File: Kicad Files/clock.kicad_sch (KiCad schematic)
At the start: 33 parts

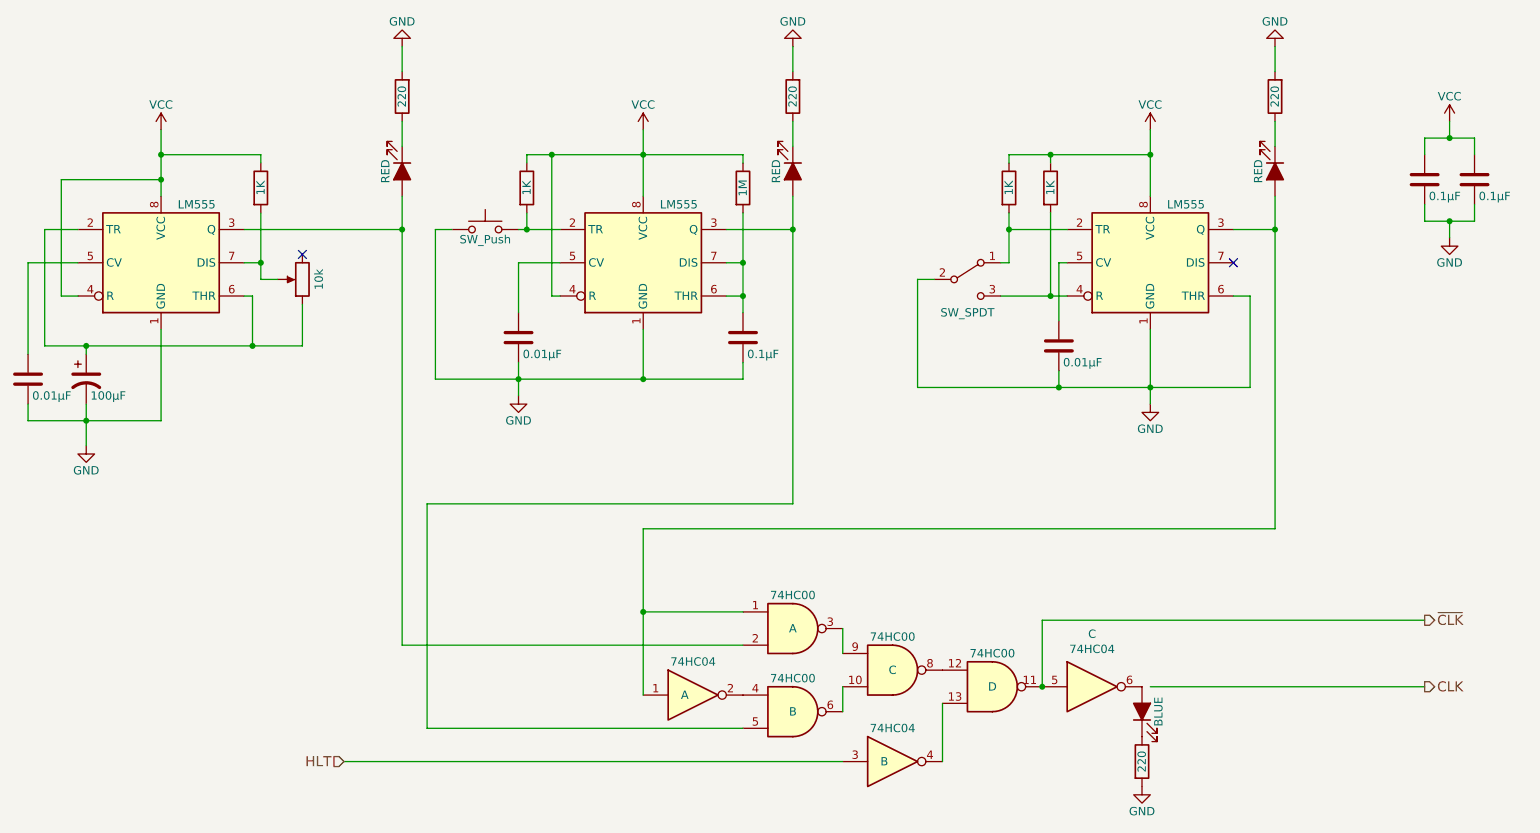
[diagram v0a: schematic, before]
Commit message: started tidy up in control
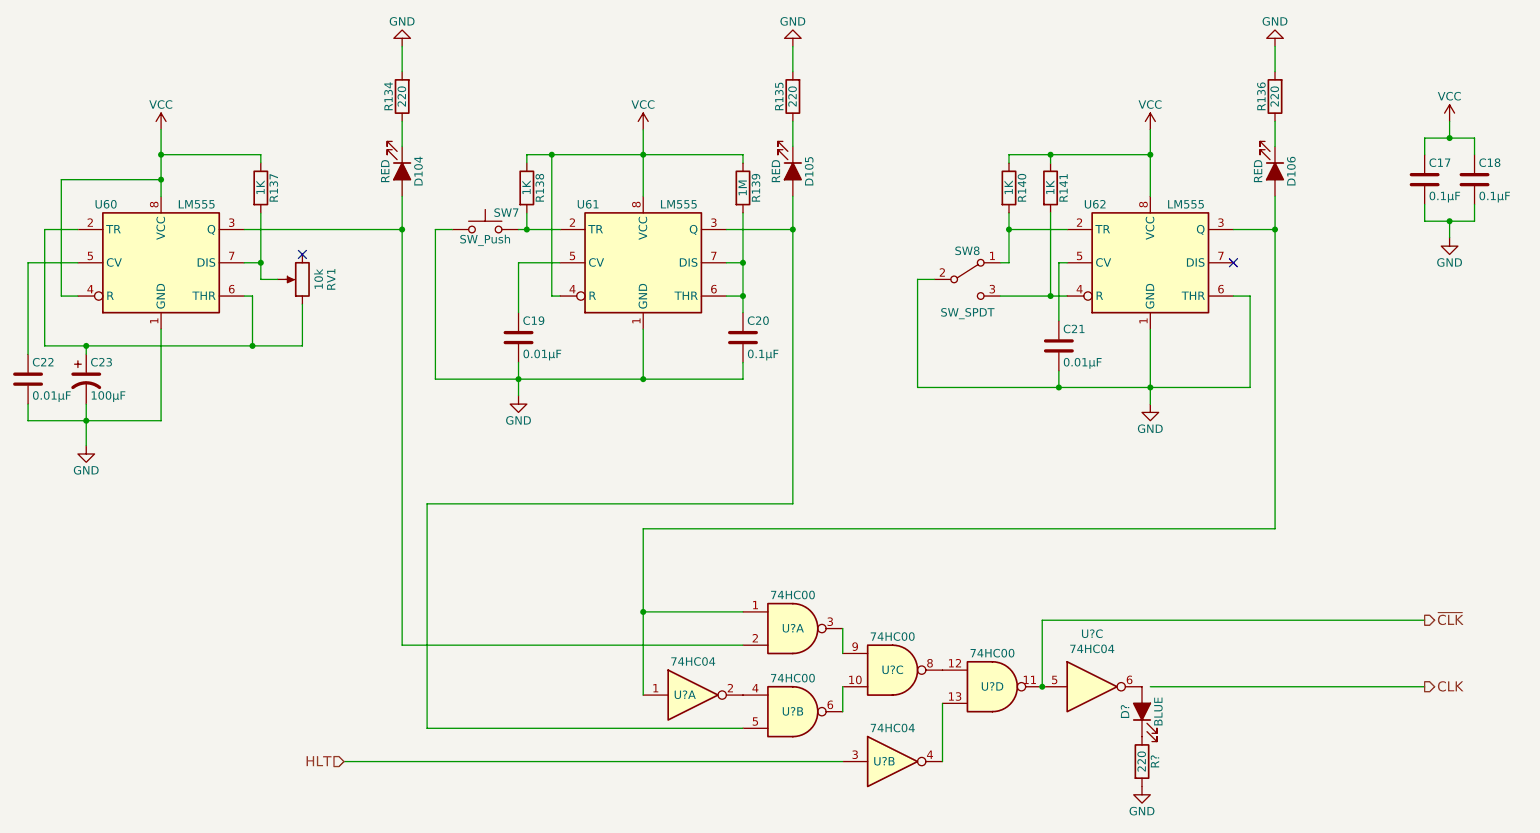
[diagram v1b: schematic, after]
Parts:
- gave numbers to parts that had none: 27

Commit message: work on cl
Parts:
- C3: renamed from C22; value 0.01µF -> C
- C5: renamed from C19; value 0.01µF -> C
- C6: renamed from C20; value 0.1µF -> C
- C7: renamed from C21; value 0.01µF -> C
- C8: renamed from C17; value 0.1µF -> C
- C9: renamed from C18; value 0.1µF -> C
- R37: renamed from R137; value 1K -> R
- R38: renamed from R134; value 220 -> R
- R39: renamed from R138; value 1K -> R
- R40: renamed from R139; value 1M -> R
- R41: renamed from R135; value 220 -> R
- R42: renamed from R140; value 1K -> R
- R43: renamed from R141; value 1K -> R
- R44: renamed from R?; value 220 -> R
- R45: renamed from R136; value 220 -> R
- gave numbers to parts that had none: 3
- renumbered C23 to C4, D104 to D12, D105 to D13, D106 to D15, SW7 to SW6, SW8 to SW7, U62 to U12, U60 to U8, U61 to U9

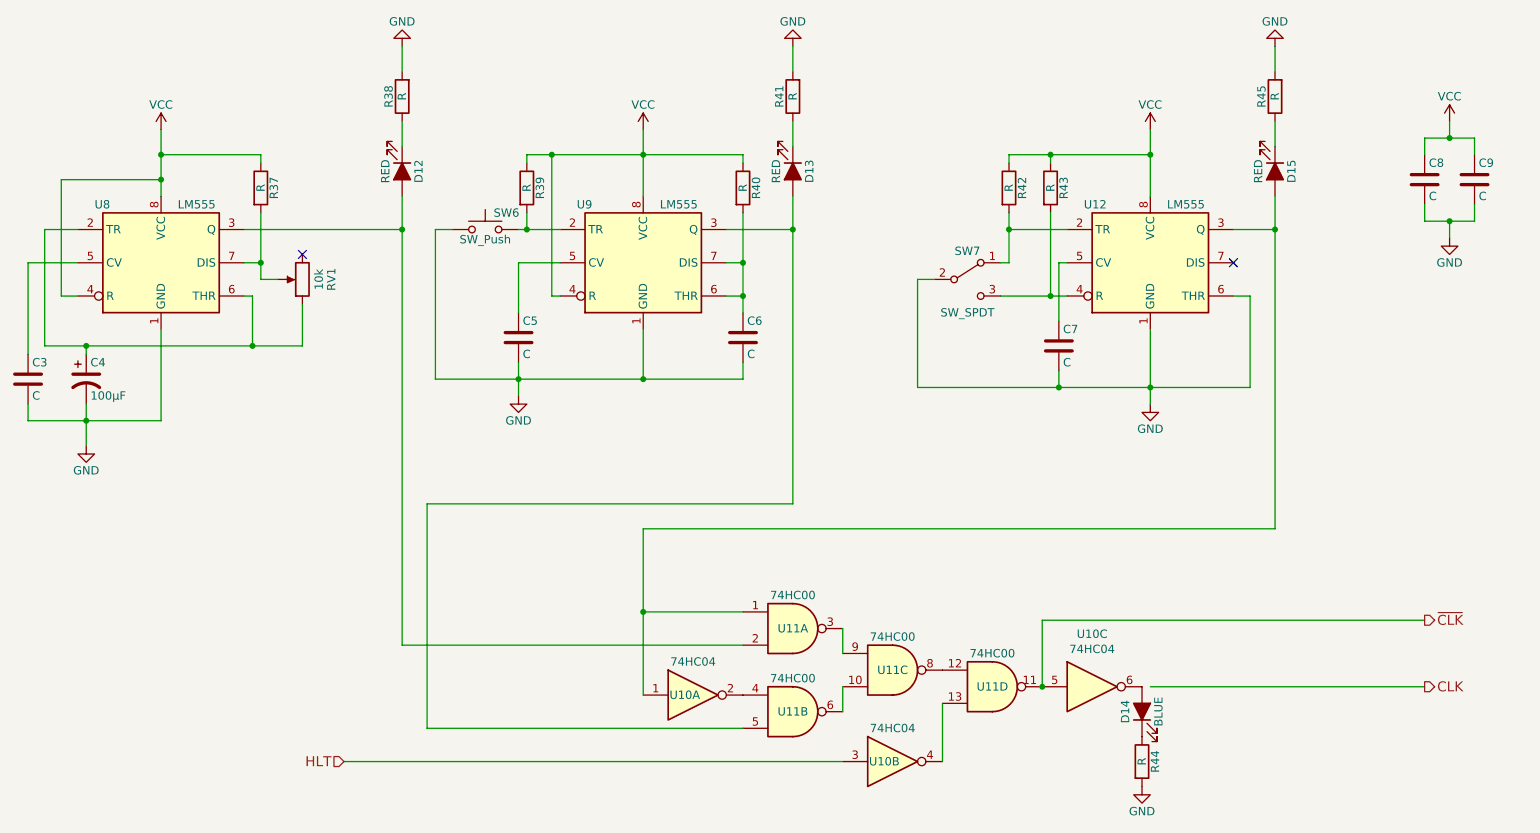
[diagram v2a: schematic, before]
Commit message: fixed ecc problems
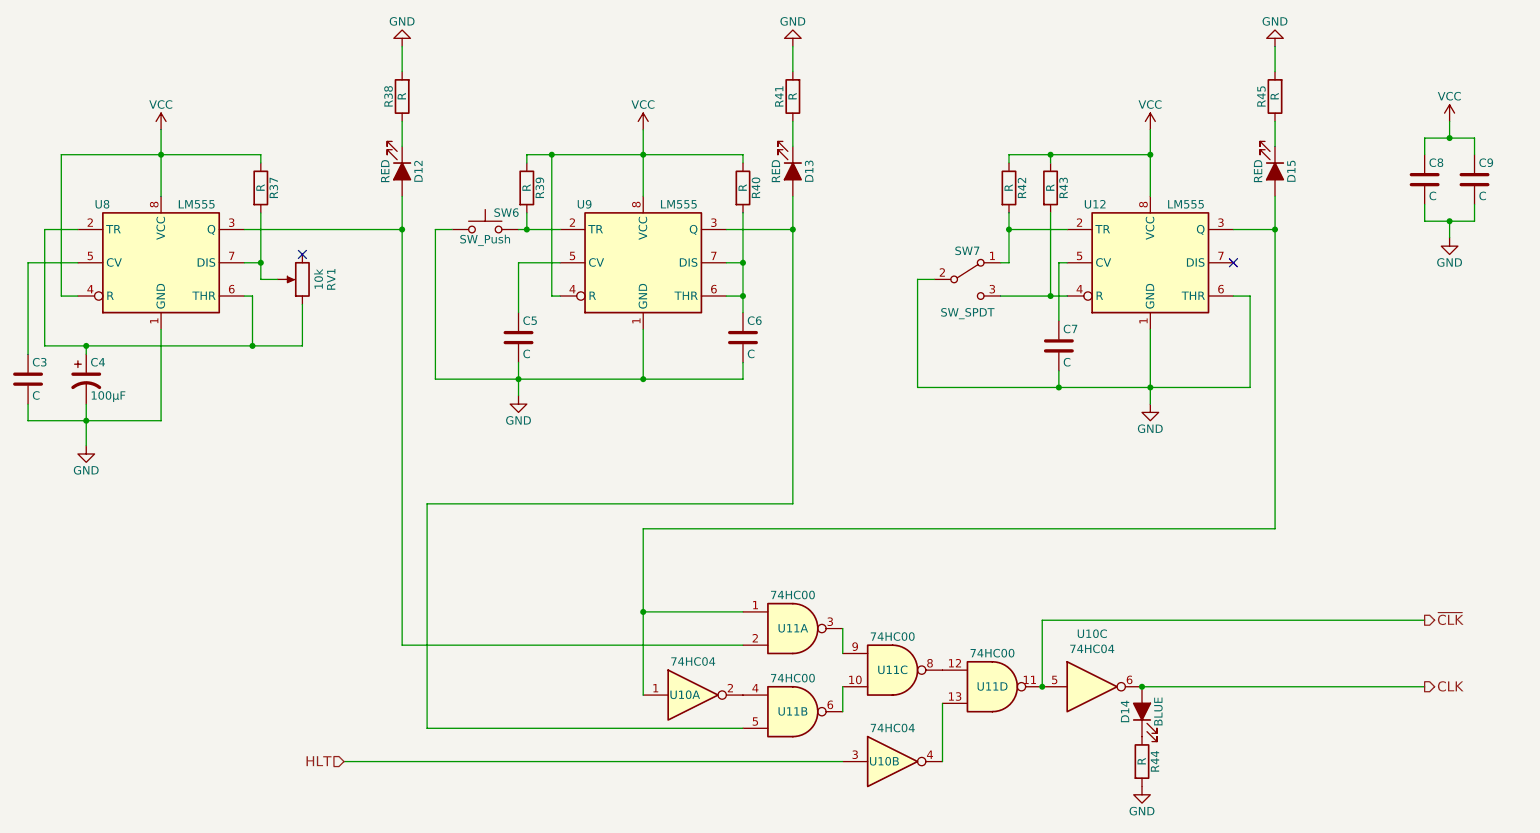
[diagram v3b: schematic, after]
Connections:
- net CLK: now also D14.2 (A), U10.6
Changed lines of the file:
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@@
   (junction (at 247.65 46.99) (diameter 0) (color 0 0 0 0)
   )
-  (junction (at 50.8 40.64) (diameter 0) (color 0 0 0 0)
-  )
   (junction (at 247.65 34.29) (diameter 0) (color 0 0 0 0)
   )
@@
   )
   (junction (at 87.63 48.26) (diameter 0) (color 0 0 0 0)
+  )
+  (junction (at 200.66 118.11) (diameter 0) (color 0 0 0 0)
   )
   (junction (at 124.46 71.12) (diameter 0) (color 0 0 0 0)
@@
     (stroke (width 0) (type default) (color 0 0 0 0))
   )
-  (wire (pts (xy 35.56 58.42) (xy 35.56 40.64))
+  (wire (pts (xy 35.56 58.42) (xy 35.56 36.83))
     (stroke (width 0) (type default) (color 0 0 0 0))
   )
@@
     (stroke (width 0) (type default) (color 0 0 0 0))
   )
-  (wire (pts (xy 201.93 118.11) (xy 243.84 118.11))
+  (wire (pts (xy 200.66 118.11) (xy 243.84 118.11))
     (stroke (width 0) (type default) (color 0 0 0 0))
   )
@@
     (stroke (width 0) (type default) (color 0 0 0 0))
   )
-  (wire (pts (xy 35.56 40.64) (xy 50.8 40.64))
+  (wire (pts (xy 35.56 36.83) (xy 50.8 36.83))
     (stroke (width 0) (type default) (color 0 0 0 0))
   )
@@
     (stroke (width 0) (type default) (color 0 0 0 0))
   )
-  (wire (pts (xy 50.8 36.83) (xy 50.8 40.64))
+  (wire (pts (xy 50.8 36.83) (xy 50.8 43.18))
     (stroke (width 0) (type default) (color 0 0 0 0))
   )
@@
     (stroke (width 0) (type default) (color 0 0 0 0))
   )
-  (wire (pts (xy 50.8 40.64) (xy 50.8 43.18))
-    (stroke (width 0) (type default) (color 0 0 0 0))
-  )

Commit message: fixed erc
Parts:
- renumbered D12 to D33, D13 to D34, D14 to D35, D15 to D36, R37 to R33, R38 to R34, R39 to R35, R40 to R36, R41 to R37, R42 to R38, R43 to R39, R44 to R40, R45 to R41, SW6 to SW1, SW7 to SW2, U8 to U4, U9 to U5, U10 to U6, U11 to U7, U12 to U8
